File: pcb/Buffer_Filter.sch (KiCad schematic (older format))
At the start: 18 parts, among them Q6 MMBT3904, Q7 BFR540, Q8 BFR540

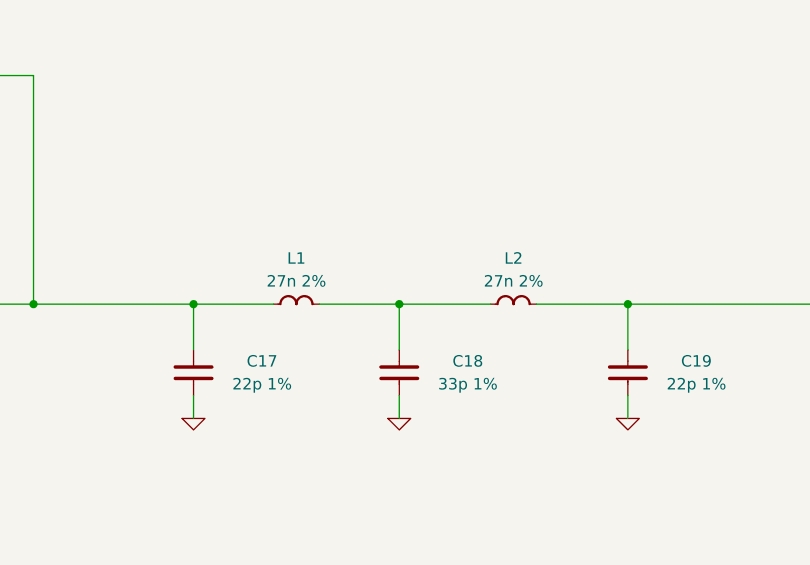
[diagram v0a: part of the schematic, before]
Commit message: Adjusted filter for proper Chebyshev response
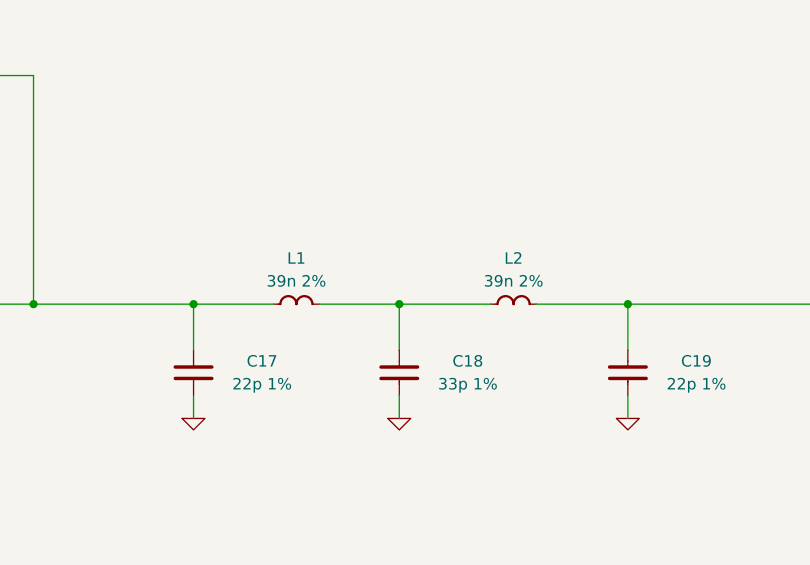
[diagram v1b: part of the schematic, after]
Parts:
- L1, L2: value 27n 2% -> 39n 2%; PN ELJ-RF27NGFB -> ELJ-RF39NGFB
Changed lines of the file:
@@
 P 6350 3600
 F 0 "L1" V 6150 3600 50  0000 C CNN
-F 1 "27n 2%" V 6250 3600 50  0000 C CNN
+F 1 "39n 2%" V 6250 3600 50  0000 C CNN
 F 2 "IPC7351-Nominal:INDC1005X60" H 6350 3650 60  0001 C CNN
 F 3 "" H 6350 3650 60  0000 C CNN
-F 4 "ELJ-RF27NGFB" H 6350 3600 60  0001 C CNN "PN"
+F 4 "ELJ-RF39NGFB" H 6350 3600 60  0001 C CNN "PN"
 F 5 "Value" H 6350 3600 60  0001 C CNN "Manuf"
 	1    6350 3600
@@
 P 7300 3600
 F 0 "L2" V 7100 3600 50  0000 C CNN
-F 1 "27n 2%" V 7200 3600 50  0000 C CNN
+F 1 "39n 2%" V 7200 3600 50  0000 C CNN
 F 2 "IPC7351-Nominal:INDC1005X60" H 7300 3650 60  0001 C CNN
 F 3 "" H 7300 3650 60  0000 C CNN
-F 4 "ELJ-RF27NGFB" H 7300 3600 60  0001 C CNN "PN"
+F 4 "ELJ-RF39NGFB" H 7300 3600 60  0001 C CNN "PN"
 F 5 "Value" H 7300 3600 60  0001 C CNN "Manuf"
 	1    7300 3600
